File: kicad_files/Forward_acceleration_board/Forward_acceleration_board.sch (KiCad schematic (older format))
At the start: 3 parts

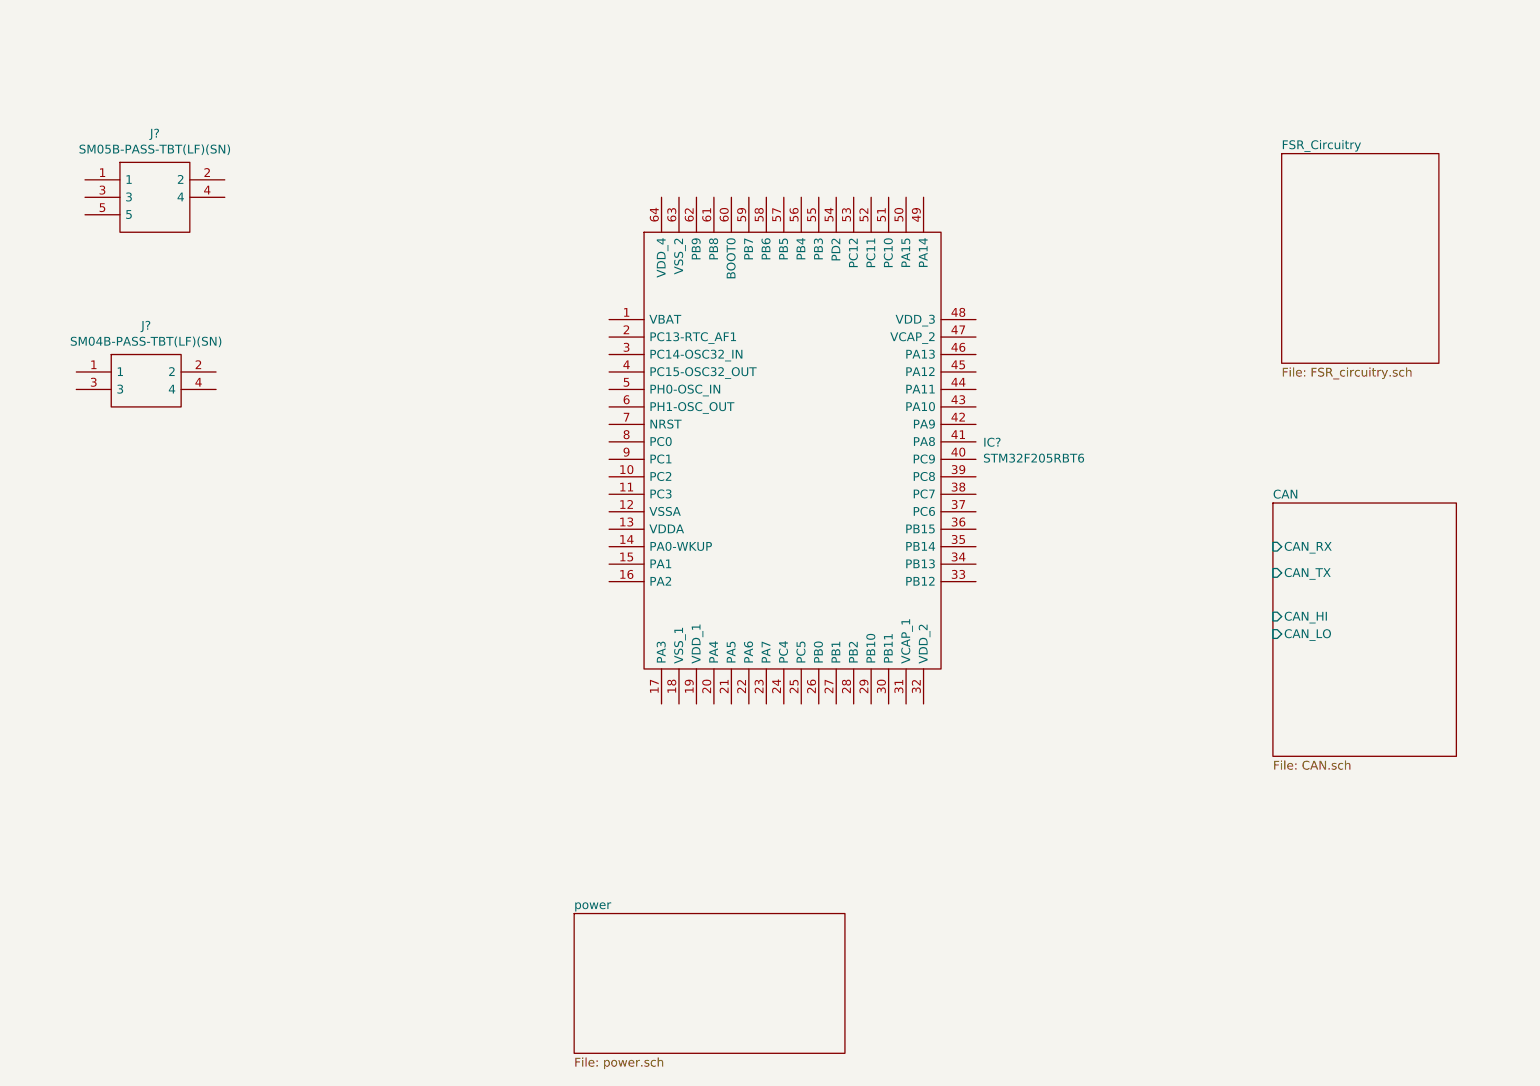
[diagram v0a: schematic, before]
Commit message: reogranized file locations, improved DSC controller pcb with edged margin on edges and rounded corners.  Completed Acceleration control board schematic
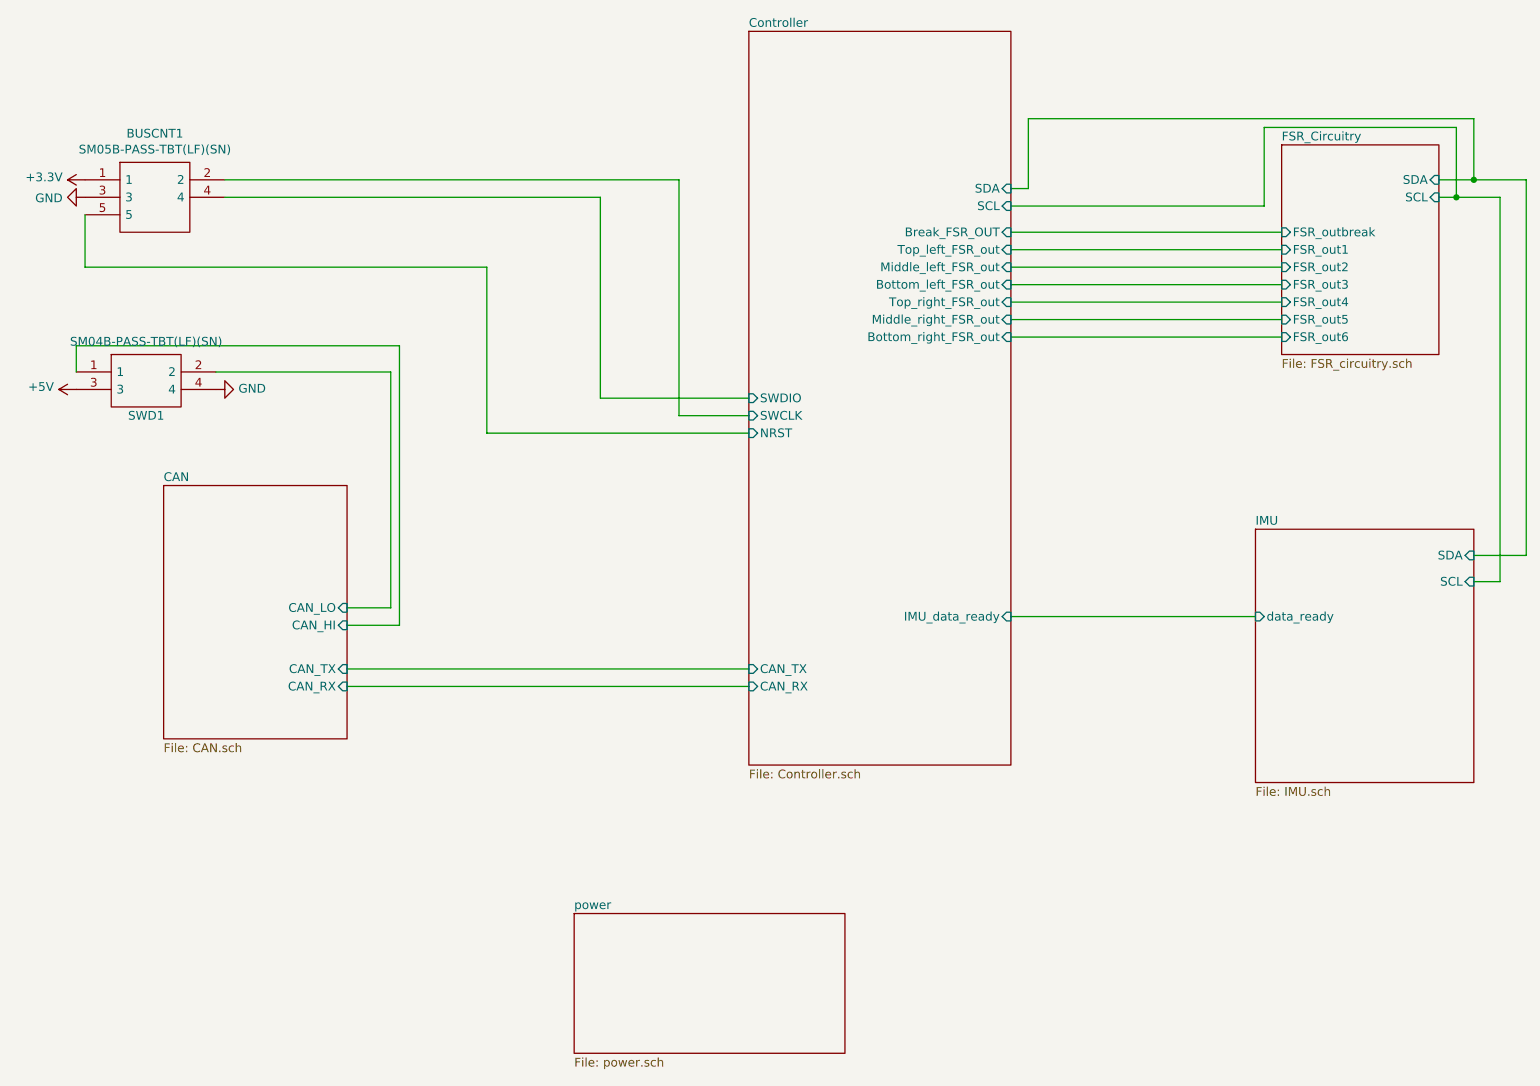
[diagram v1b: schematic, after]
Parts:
- removed IC?: STM32F205RBT6, QFP50P1200X1200X160-64N, symbol STM32F205RBT6:STM32F205RBT6
- BUSCNT1: renamed from J?; footprint SM05BPASSTBTLFSN -> SM05B-PASS-TBT(LF)(SN):SM05BPASSTBTLFSN
- SWD1: renamed from J?; footprint SM04B-PASS-TBT -> SM04B-PASS-TBT(LF)(SN):SM04B-PASS-TBT
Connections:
- net CAN/CAN_HI: now also SWD1.1
- net CAN/CAN_LO: now also SWD1.2
- net +3V3: now reaches BUSCNT1.1
- net Controller/SWCLK: now reaches BUSCNT1.2
- net GND: now reaches BUSCNT1.3
- net GND: now also SWD1.4
- net Controller/SWDIO: now reaches BUSCNT1.4
- net Controller/NRST: now reaches BUSCNT1.5
- net +5V: now reaches SWD1.3
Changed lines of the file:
@@
 $Descr A4 11693 8268
 encoding utf-8
-Sheet 1 4
+Sheet 1 6
 Title ""
 Date ""
@@
 $EndDescr
 $Sheet
-S 7850 2100 900  1200
+S 7850 2050 900  1200
 U 5D8CBEA0
 F0 "FSR_Circuitry" 50
 F1 "FSR_circuitry.sch" 50
-$EndSheet
-$Sheet
-S 7800 4100 1050 1450
+F2 "SDA" I R 8750 2250 50
+F3 "SCL" I R 8750 2350 50
+F4 "FSR_out5" I L 7850 3050 50
+F5 "FSR_out6" I L 7850 3150 50
+F6 "FSR_out1" I L 7850 2650 50
+F7 "FSR_out2" I L 7850 2750 50
+F8 "FSR_out4" I L 7850 2950 50
+F9 "FSR_out3" I L 7850 2850 50
+F10 "FSR_outbreak" I L 7850 2550 50
+$EndSheet
+$Sheet
+S 1450 4000 1050 1450
 U 5D8CBEE6
 F0 "CAN" 50
 F1 "CAN.sch" 50
-F2 "CAN_RX" I L 7800 4350 50
-F3 "CAN_TX" I L 7800 4500 50
-F4 "CAN_HI" I L 7800 4750 50
-F5 "CAN_LO" I L 7800 4850 50
-$EndSheet
-$Comp
-L STM32F205RBT6:STM32F205RBT6 IC?
-U 1 1 5D8CCE19
-P 4000 3050
-F 0 "IC?" H 6141 2346 50  0000 L CNN
-F 1 "STM32F205RBT6" H 6141 2255 50  0000 L CNN
-F 2 "QFP50P1200X1200X160-64N" H 5950 3550 50  0001 L CNN
-F 3 "https://componentsearchengine.com/Datasheets/1/STM32F205RBT6.pdf" H 5950 3450 50  0001 L CNN
-F 4 "" H 5950 3350 50  0001 L CNN "Description"
-F 5 "1.6" H 5950 3250 50  0001 L CNN "Height"
-F 6 "511-STM32F205RBT6" H 5950 3150 50  0001 L CNN "Mouser Part Number"
-F 7 "https://www.mouser.com/Search/Refine.aspx?Keyword=511-STM32F205RBT6" H 5950 3050 50  0001 L CNN "Mouser Price/Stock"
-F 8 "STMicroelectronics" H 5950 2950 50  0001 L CNN "Manufacturer_Name"
-F 9 "STM32F205RBT6" H 5950 2850 50  0001 L CNN "Manufacturer_Part_Number"
-	1    4000 3050
-	1    0    0    -1
-$EndComp
-$Comp
-L SM05B-PASS-TBT(LF)(SN):SM05B-PASS-TBT(LF)(SN) J?
+F2 "CAN_RX" I R 2500 5150 50
+F3 "CAN_TX" I R 2500 5050 50
+F4 "CAN_HI" I R 2500 4800 50
+F5 "CAN_LO" I R 2500 4700 50
+$EndSheet
+$Comp
+L SM05B-PASS-TBT(LF)(SN):SM05B-PASS-TBT(LF)(SN) BUSCNT1
 U 1 1 5D8CD028
 P 1000 2250
-F 0 "J?" H 1400 2515 50  0000 C CNN
+F 0 "BUSCNT1" H 1400 2515 50  0000 C CNN
 F 1 "SM05B-PASS-TBT(LF)(SN)" H 1400 2424 50  0000 C CNN
-F 2 "SM05BPASSTBTLFSN" H 1650 2350 50  0001 L CNN
+F 2 "SM05B-PASS-TBT(LF)(SN):SM05BPASSTBTLFSN" H 1650 2350 50  0001 L CNN
 F 3 "http://www.jst-mfg.com/product/pdf/eng/ePA-F.pdf" H 1650 2250 50  0001 L CNN
 F 4 "CONN HEADER PA 5POS SIDE SMD" H 1650 2150 50  0001 L CNN "Description"
@@
 $EndComp
 $Comp
-L SM04B-PASS-TBT(LF)(SN):SM04B-PASS-TBT(LF)(SN) J?
+L SM04B-PASS-TBT(LF)(SN):SM04B-PASS-TBT(LF)(SN) SWD1
 U 1 1 5D8CD619
 P 950 3350
-F 0 "J?" H 1350 3615 50  0000 C CNN
+F 0 "SWD1" H 1350 3100 50  0000 C CNN
 F 1 "SM04B-PASS-TBT(LF)(SN)" H 1350 3524 50  0000 C CNN
-F 2 "SM04B-PASS-TBT" H 1600 3450 50  0001 L CNN
+F 2 "SM04B-PASS-TBT(LF)(SN):SM04B-PASS-TBT" H 1600 3450 50  0001 L CNN
 F 3 "http://www.jst-mfg.com/product/pdf/eng/ePA-F.pdf" H 1600 3350 50  0001 L CNN
 F 4 "JST (JAPAN SOLDERLESS TERMINALS) - SM04B-PASS-TBT(LF)(SN) - CONNECTOR, HEADER, 4POS, 1ROW, 2MM" H 1600 3250 50  0001 L CNN "Description"
@@
 F1 "power.sch" 50
 $EndSheet
+Wire Wire Line
+	2500 4700 2750 4700
+Wire Wire Line
+	2750 4700 2750 3350
+Wire Wire Line
+	2750 3350 1750 3350
+Wire Wire Line
+	950  3350 950  3200
+Wire Wire Line
+	950  3200 2800 3200
+Wire Wire Line
+	2800 3200 2800 4800
+Wire Wire Line
+	2800 4800 2500 4800
+$Comp
+L power:+5V #PWR0101
+U 1 1 5D9DC2E8
+P 950 3450
+F 0 "#PWR0101" H 950 3300 50  0001 C CNN
+F 1 "+5V" V 965 3578 50  0000 L CNN
+F 2 "" H 950 3450 50  0001 C CNN
+F 3 "" H 950 3450 50  0001 C CNN
+	1    950  3450
+	0    -1   -1   0
+$EndComp
+$Comp
+L power:GND #PWR0102
+U 1 1 5D9DC35B
+P 1750 3450
+F 0 "#PWR0102" H 1750 3200 50  0001 C CNN
+F 1 "GND" V 1755 3322 50  0000 R CNN
+F 2 "" H 1750 3450 50  0001 C CNN
+F 3 "" H 1750 3450 50  0001 C CNN
+	1    1750 3450
+	0    -1   -1   0
+$EndComp
+Wire Wire Line
+	3300 3700 3300 2750
+Wire Wire Line
+	3300 2750 1000 2750
+Wire Wire Line
+	1000 2750 1000 2450
+$Comp
+L power:+3.3V #PWR0103
+U 1 1 5D9DC45A
+P 1000 2250
+F 0 "#PWR0103" H 1000 2100 50  0001 C CNN
+F 1 "+3.3V" V 1015 2378 50  0000 L CNN
+F 2 "" H 1000 2250 50  0001 C CNN
+F 3 "" H 1000 2250 50  0001 C CNN
+	1    1000 2250
+	0    -1   -1   0
+$EndComp
+$Sheet
+S 4800 1400 1500 4200
+U 5D9E49EF
+F0 "Controller" 50
+F1 "Controller.sch" 50
+F2 "NRST" I L 4800 3700 50
+F3 "Top_left_FSR_out" I R 6300 2650 50
+F4 "Middle_left_FSR_out" I R 6300 2750 50
+F5 "Bottom_left_FSR_out" I R 6300 2850 50
+F6 "Break_FSR_OUT" I R 6300 2550 50
+F7 "Top_right_FSR_out" I R 6300 2950 50
+F8 "Middle_right_FSR_out" I R 6300 3050 50
+F9 "Bottom_right_FSR_out" I R 6300 3150 50
+F10 "IMU_data_ready" I R 6300 4750 50
+F11 "SDA" I R 6300 2300 50
+F12 "SCL" I R 6300 2400 50
+F13 "CAN_TX" I L 4800 5050 50
+F14 "CAN_RX" I L 4800 5150 50
+F15 "SWCLK" I L 4800 3600 50
+F16 "SWDIO" I L 4800 3500 50
+$EndSheet
+$Sheet
+S 7700 4250 1250 1450
+U 5D9E4F5D
+F0 "IMU" 50
+F1 "IMU.sch" 50
+F2 "SDA" I R 8950 4400 50
+F3 "SCL" I R 8950 4550 50
+F4 "data_ready" I L 7700 4750 50
+$EndSheet
+Wire Wire Line
+	3300 3700 4800 3700
+Wire Wire Line
+	6300 2550 7850 2550
+Wire Wire Line
+	6300 2650 7850 2650
+Wire Wire Line
+	6300 2750 7850 2750
+Wire Wire Line
+	6300 2850 7850 2850
+Wire Wire Line
+	6300 2950 7850 2950
+Wire Wire Line
+	6300 3050 7850 3050
+Wire Wire Line
+	6300 3150 7850 3150
+Wire Wire Line
+	7700 4750 6300 4750
+Wire Wire Line
+	6300 2300 6400 2300
+Wire Wire Line
+	6400 2300 6400 1900
+Wire Wire Line
+	6400 1900 8950 1900
+Wire Wire Line
+	8950 1900 8950 2250
+Wire Wire Line
+	8950 2250 8750 2250
+Wire Wire Line
+	6300 2400 7750 2400
+Wire Wire Line
+	7750 2400 7750 1950
+Wire Wire Line
+	7750 1950 8850 1950
+Wire Wire Line
+	8850 1950 8850 2350
+Wire Wire Line
+	8850 2350 8750 2350
+Wire Wire Line
+	8850 2350 9100 2350
+Wire Wire Line
+	9100 2350 9100 4550
+Wire Wire Line
+	9100 4550 8950 4550
+Connection ~ 8850 2350
+Wire Wire Line
+	8950 4400 9250 4400
+Wire Wire Line
+	9250 4400 9250 2250
+Wire Wire Line
+	9250 2250 8950 2250
+Connection ~ 8950 2250
+Wire Wire Line
+	4800 5050 2500 5050
+Wire Wire Line
+	4800 5150 2500 5150
+$Comp
+L power:GND #PWR0104
+U 1 1 5DAFEC73
+P 1000 2350
+F 0 "#PWR0104" H 1000 2100 50  0001 C CNN
+F 1 "GND" V 1005 2222 50  0000 R CNN
+F 2 "" H 1000 2350 50  0001 C CNN
+F 3 "" H 1000 2350 50  0001 C CNN
+	1    1000 2350
+	0    1    1    0
+$EndComp
+Wire Wire Line
+	4800 3600 4400 3600
+Wire Wire Line
+	4400 3600 4400 2250
+Wire Wire Line
+	4400 2250 1800 2250
+Wire Wire Line
+	4800 3500 3950 3500
+Wire Wire Line
+	3950 3500 3950 2350
+Wire Wire Line
+	3950 2350 1800 2350
 $EndSCHEMATC
